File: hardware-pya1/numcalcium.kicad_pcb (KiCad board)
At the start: 2 copper layers, 77.6 x 161.1 mm, 142 parts, among them J1 Conn_01x14_Socket, J2 Conn_01x14_Socket, J3 LCD_socket, J4 Micro_SD_Card_Det2, J5 AudioJack4, J6 USB_C_Receptacle_USB2.0_16P, J7 Conn_02x08_Odd_Even, Q1 AO3401A, Q2 BSS138, Q3 AO3401A, Q5 AO4953A, Q6 BSS138, Q8 BSS138, Q9 BSS138, SW1 SW_Push, SW10 SW_Push, SW11 SW_Push, SW12 SW_Push, SW13 SW_Push, SW14 SW_Push, SW15 SW_Push, SW16 SW_Push, SW17 SW_Push, SW18 SW_Push, SW19 SW_Push, SW2 SW_Push, SW20 SW_Push, SW21 Encoder, SW22 SW_Push, SW3 SW_Push, SW4 SW_Push, SW5 SW_Push, SW6 SW_Push, SW7 SW_Push, SW8 SW_Push, SW9 SW_Push, U1 LTC4054, U2 STI3411A, U3 74HC595, U4 ESP32-S3-WROOM-1, U5 XC6206PxxxMR

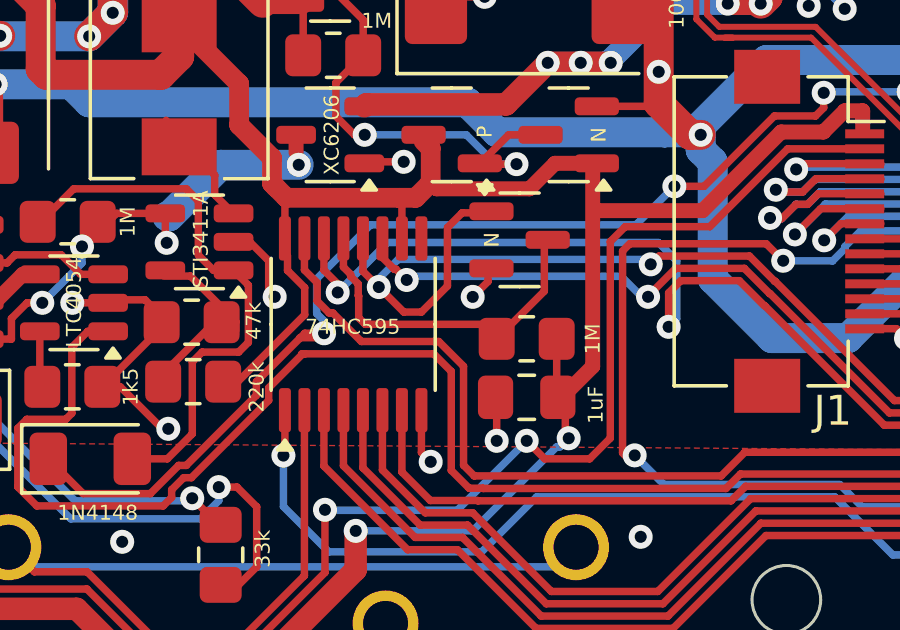
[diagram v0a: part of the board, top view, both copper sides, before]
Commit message: all: fix sleep in sw and hw but hw layout prevents keyscanning in sleep Need to find a way to sniff GPIO0 in sleep
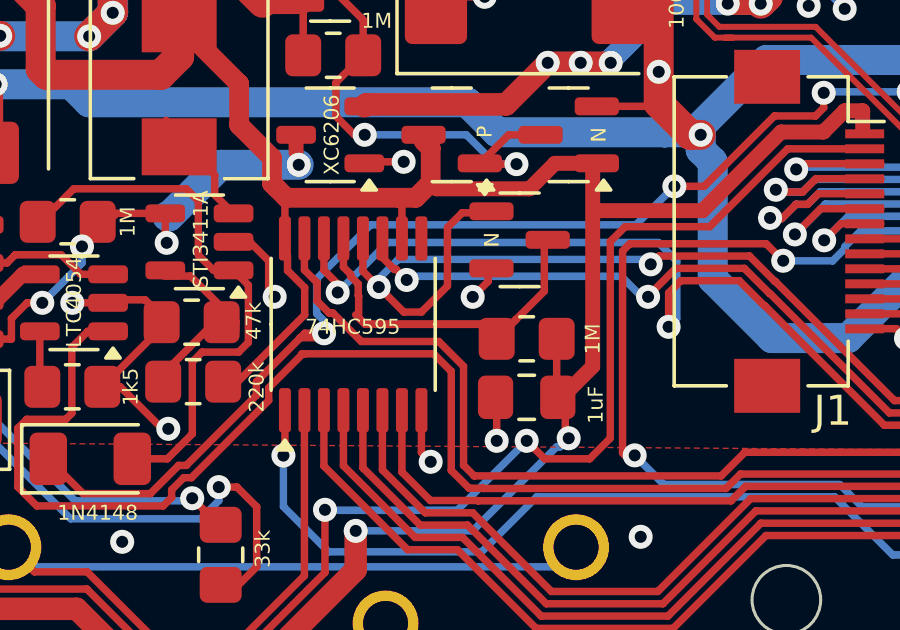
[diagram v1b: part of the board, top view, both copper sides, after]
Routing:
- net Net-(Q6-D): track 11.7 -> 17.2 mm

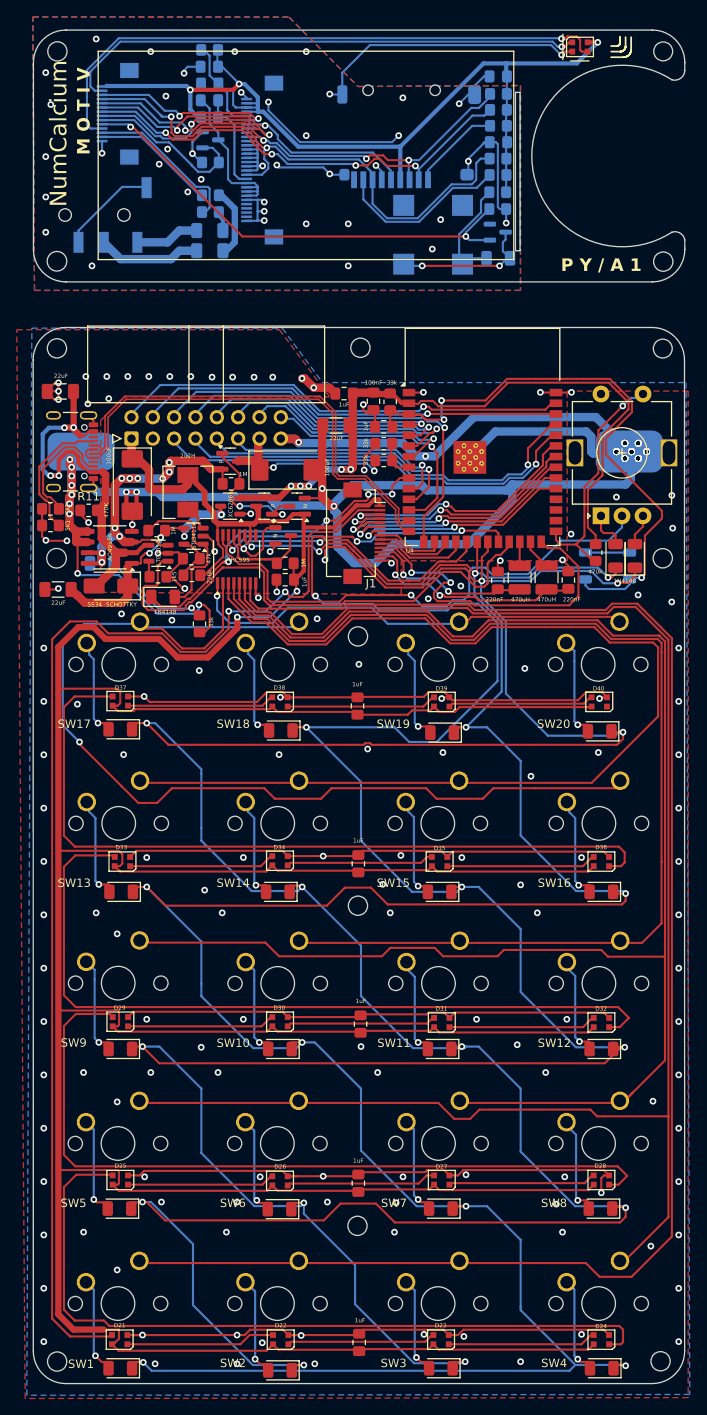
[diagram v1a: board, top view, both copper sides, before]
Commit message: pcb: redesign fix for LowPowerReq - added passives optional cap for slowstart on regulator switching to hi-power
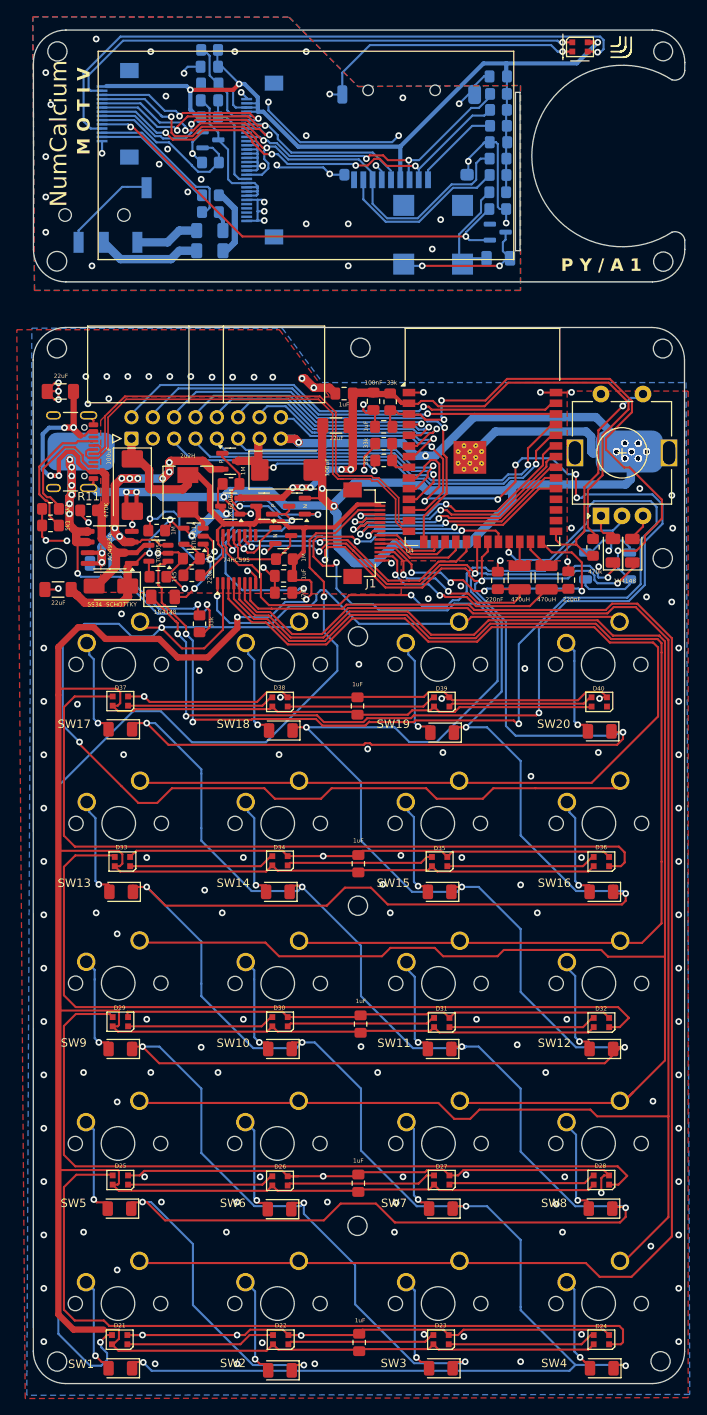
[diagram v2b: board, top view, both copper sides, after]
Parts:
- added C24: 470n, Capacitor_SMD:C_0805_2012Metric_Pad1.18x1.45mm_HandSolder, F.Cu at (29.3, 22.9)
- moved D45 0.69 mm to (68.5, 17.9)
- moved D46 0.69 mm to (70.8, 17.9)
- moved R12 0.69 mm to (66.1, 17.5)
- moved R10 0.51 mm to (29.4, 18.9)
- moved C5 0.49 mm to (29.3, 20.9)
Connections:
- net SYSTEM_ON_CTRL renamed Net-(Q1-G)
- C22 pad 1: VCC_REG -> Net-(D43-K)
- C6 pad 1: VDD -> VDD_AON
- C7 pad 1: VDD -> VDD_AON
- C8 pad 1: VDD -> VDD_AON
- D40 pad 1: /Main/lighting/DOUT -> unconnected-(D40-DOUT-Pad1)
- D43 pad 1: VCC_REG -> Net-(D43-K)
- Q1 pad 2: VBAT_CH -> Net-(Q1-S)
- Q2 pad 1: VDD -> Net-(D44-A)
- Q3 pad 2: VDD -> VDD_AON
- Q5 pad 1: VCC_REG -> Net-(D43-K)
- Q5 pad 3: VBAT_CH -> Net-(Q1-S)
- Q5 pad 7: VBAT_CH -> Net-(Q1-S)
- Q5 pad 8: VBAT_CH -> Net-(Q1-S)
- R12 pad 1: VDD -> VDD_AON
- R14 pad 1: VDD -> VDD_AON
- R3 pad 1: VCC_REG -> Net-(D43-K)
- R7 pad 1: VBAT_CH -> Net-(D43-K)
- U1 pad 3: VBAT_CH -> Net-(Q1-S)
- U2 pad 4: VCC_REG -> Net-(D43-K)
- U4 pad 2: VDD -> VDD_AON
- U5 pad 2: VDD -> VDD_AON
- U5 pad 3: VCC_REG -> Net-(D43-K)
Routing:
- net #LOW_POWER_REQ: track 40.9 -> 140.0 mm, vias 4 -> 8
- net VDD_AON: track 0.00 -> 82.4 mm, vias 0 -> 5
- net VDD: track 609.5 -> 527.5 mm, vias 7 -> 2
- net CHARGE_STATE: track 64.1 -> 121.8 mm, vias 0 -> 4
- net VBAT_CH: track 50.1 -> 0.00 mm, vias 10 -> 0
- net Net-(Q1-S): track 0.00 -> 48.4 mm, vias 0 -> 10
- net Net-(D43-K): track 0.00 -> 33.9 mm, vias 0 -> 4
- net VCC_REG: track 27.7 -> 0.00 mm, vias 4 -> 0
- net Net-(Q1-G): track 17.2 -> 43.3 mm, vias 2 -> 3
- net Net-(D44-A): track 18.6 -> 43.4 mm, vias 0 -> 4
- net GND: track 565.3 -> 574.6 mm, vias 265 -> 268
- net Net-(Q6-D): track 17.2 -> 10.9 mm
- net /Main/STATUS_LED: track 41.2 -> 36.8 mm, vias 2 -> 4
- net /Front/LED: track 71.2 -> 75.3 mm
- net /Main/AUD_L: track 20.4 -> 24.4 mm
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
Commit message: pcb: revert led path to allow the option of populating rgb keys or not
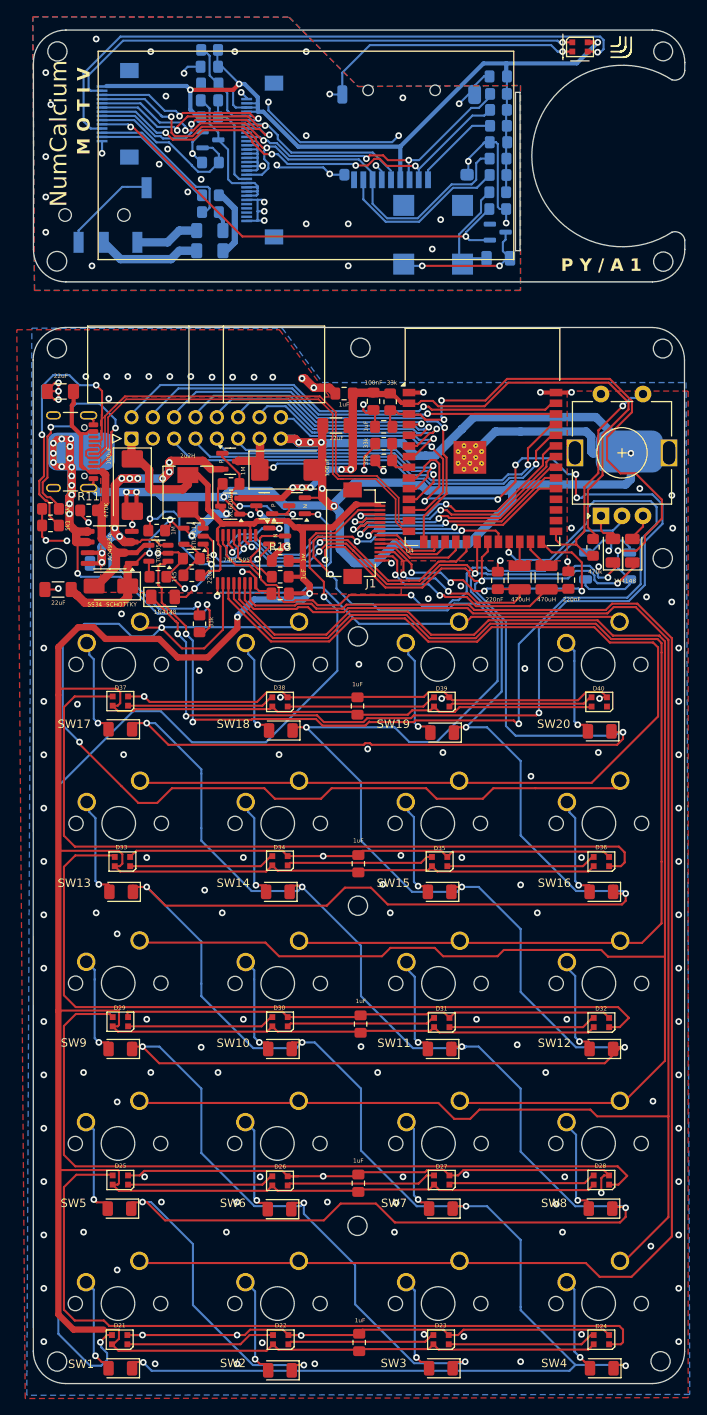
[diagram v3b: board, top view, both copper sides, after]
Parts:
- removed C24: 470n, Capacitor_SMD:C_0805_2012Metric_Pad1.18x1.45mm_HandSolder
- added R13: 22R, Resistor_SMD:R_0805_2012Metric_Pad1.20x1.40mm_HandSolder, F.Cu at (28.9, 19.1)
- moved R10 2.16 mm to (28.9, 21.0)
- moved C5 2.14 mm to (28.9, 23.0)
- moved Q6 0.73 mm to (28.5, 16.1)
- moved Q2 0.05 mm to (30.9, 12.5)
- moved Q3 0.05 mm to (27.0, 12.5)
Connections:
- Q3 pad 3: VDD -> Net-(Q3-D)
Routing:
- net Net-(Q1-G): track 43.3 -> 18.4 mm, vias 3 -> 2
- net Net-(J6-CC1): track 16.5 -> 34.0 mm, vias 0 -> 2
- net Net-(J6-CC2): track 13.9 -> 29.5 mm, vias 0 -> 2
- net VBUS: track 52.2 -> 37.3 mm, vias 4 -> 0
- net Net-(Q3-D): track 0.00 -> 10.8 mm, vias 0 -> 2
- net Net-(BT1-+): track 48.1 -> 57.6 mm, vias 9 -> 16
- net GND: track 574.6 -> 584.0 mm, vias 268 -> 155
- net IO_OE: track 39.3 -> 47.3 mm, vias 2 -> 3
- net Net-(Q6-D): track 10.9 -> 14.8 mm
- net Net-(U3-QB): track 56.4 -> 52.6 mm
- net VDD: track 527.5 -> 524.8 mm
- net Net-(D44-A): track 43.4 -> 45.4 mm
- net IO_D: track 357.3 -> 359.3 mm
- net Net-(U3-QG): track 198.2 -> 196.2 mm
- net Net-(U3-QF): track 200.9 -> 199.0 mm
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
